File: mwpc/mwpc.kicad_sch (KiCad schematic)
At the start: 132 parts, among them X1 MWPC_HVT, X2 MWPC_HVT, X3 MWPC_HVT, X4 MWPC_HVT

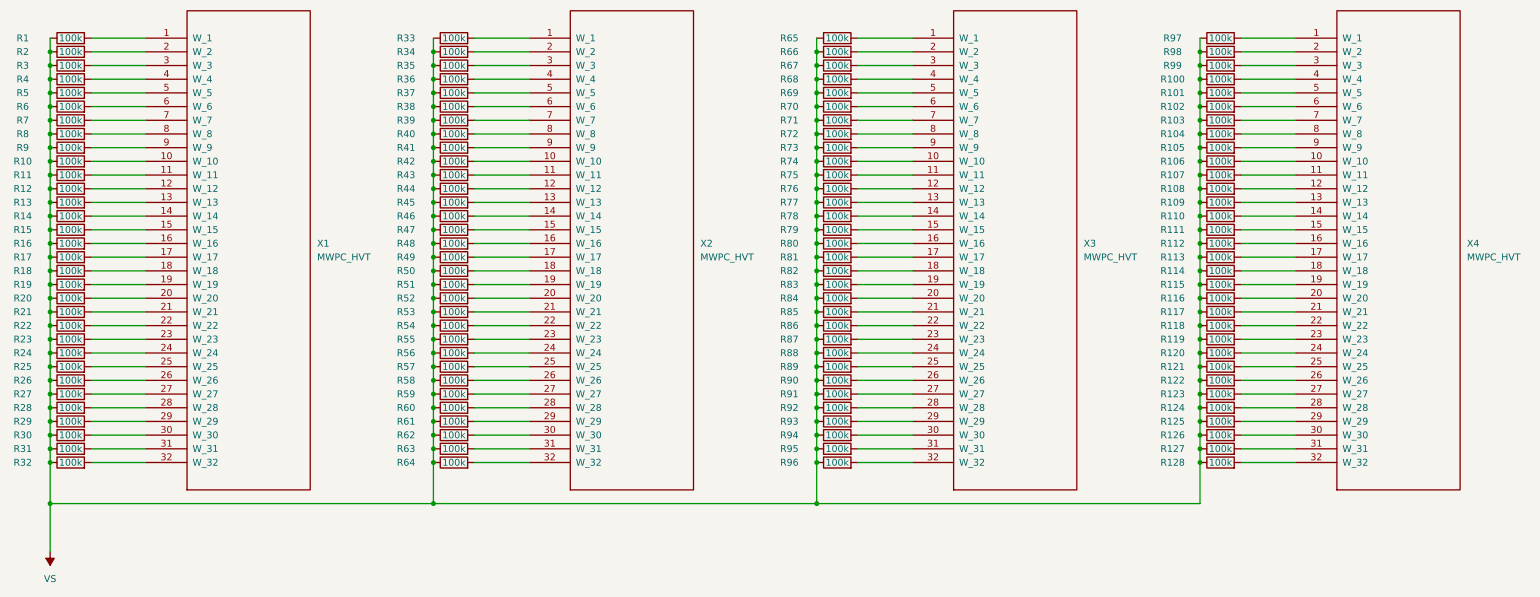
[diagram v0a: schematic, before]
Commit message: Rearrange the components on the PCB.
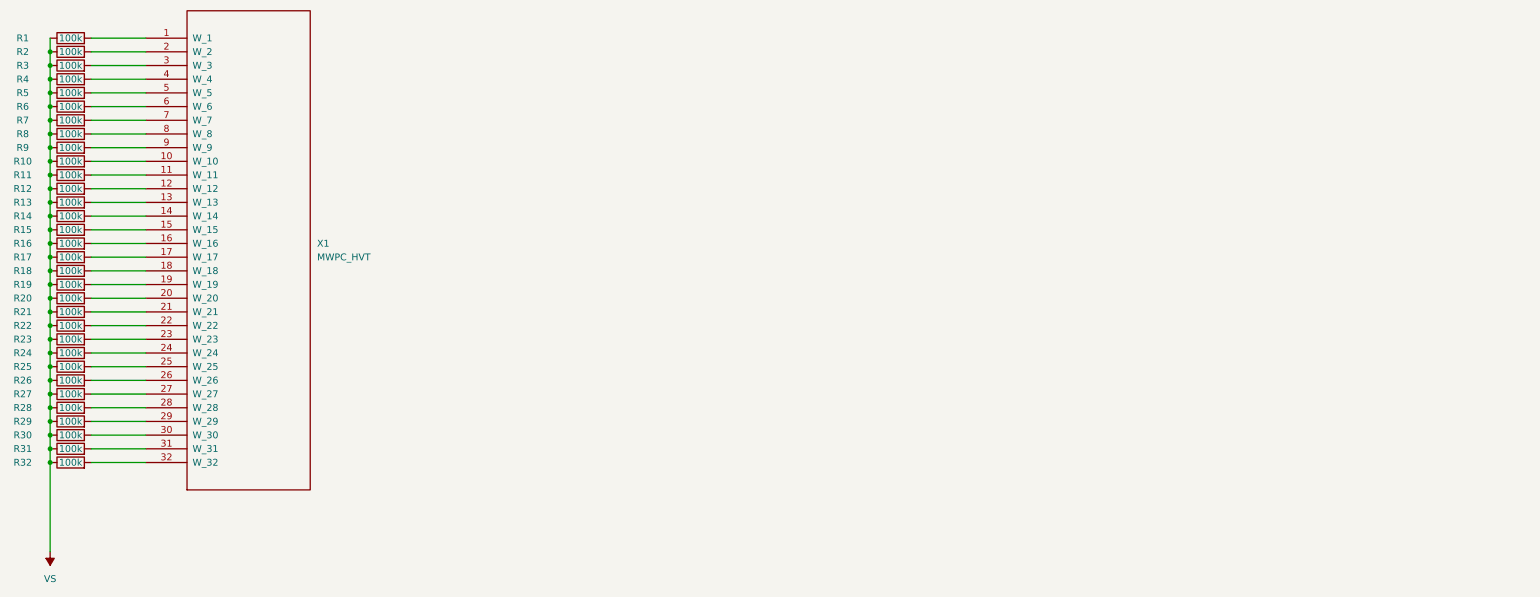
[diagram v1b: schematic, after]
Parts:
- removed R100, R101, R102, R103, R104, R105, R106, R107, R108, R109, R110, R111, R112, R113, R114, R115, R116, R117, R118, R119, R120, R121, R122, R123, R124, R125, R126, R127, R128, R33, R34, R35, R36, R37, R38, R39, R40, R41, R42, R43, R44, R45, R46, R47, R48, R49, R50, R51, R52, R53, R54, R55, R56, R57, R58, R59, R60, R61, R62, R63, R64, R65, R66, R67, R68, R69, R70, R71, R72, R73, R74, R75, R76, R77, R78, R79, R80, R81, R82, R83, R84, R85, R86, R87, R88, R89, R90, R91, R92, R93, R94, R95, R96, R97, R98, R99: 100k, Resistor_SMD:R_0201_0603Metric, symbol Device:R
- removed X2, X3, X4: MWPC_HVT, mwpc:MWPC_HVT_SMD, symbol mwpc:MWPC_HVT
